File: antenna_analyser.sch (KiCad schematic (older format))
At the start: 25 parts, among them IC1 MCP6002, P1 CONN_01X10, P2 CONN_01X10, P3 CONN_01X04, P4 CONN_01X02

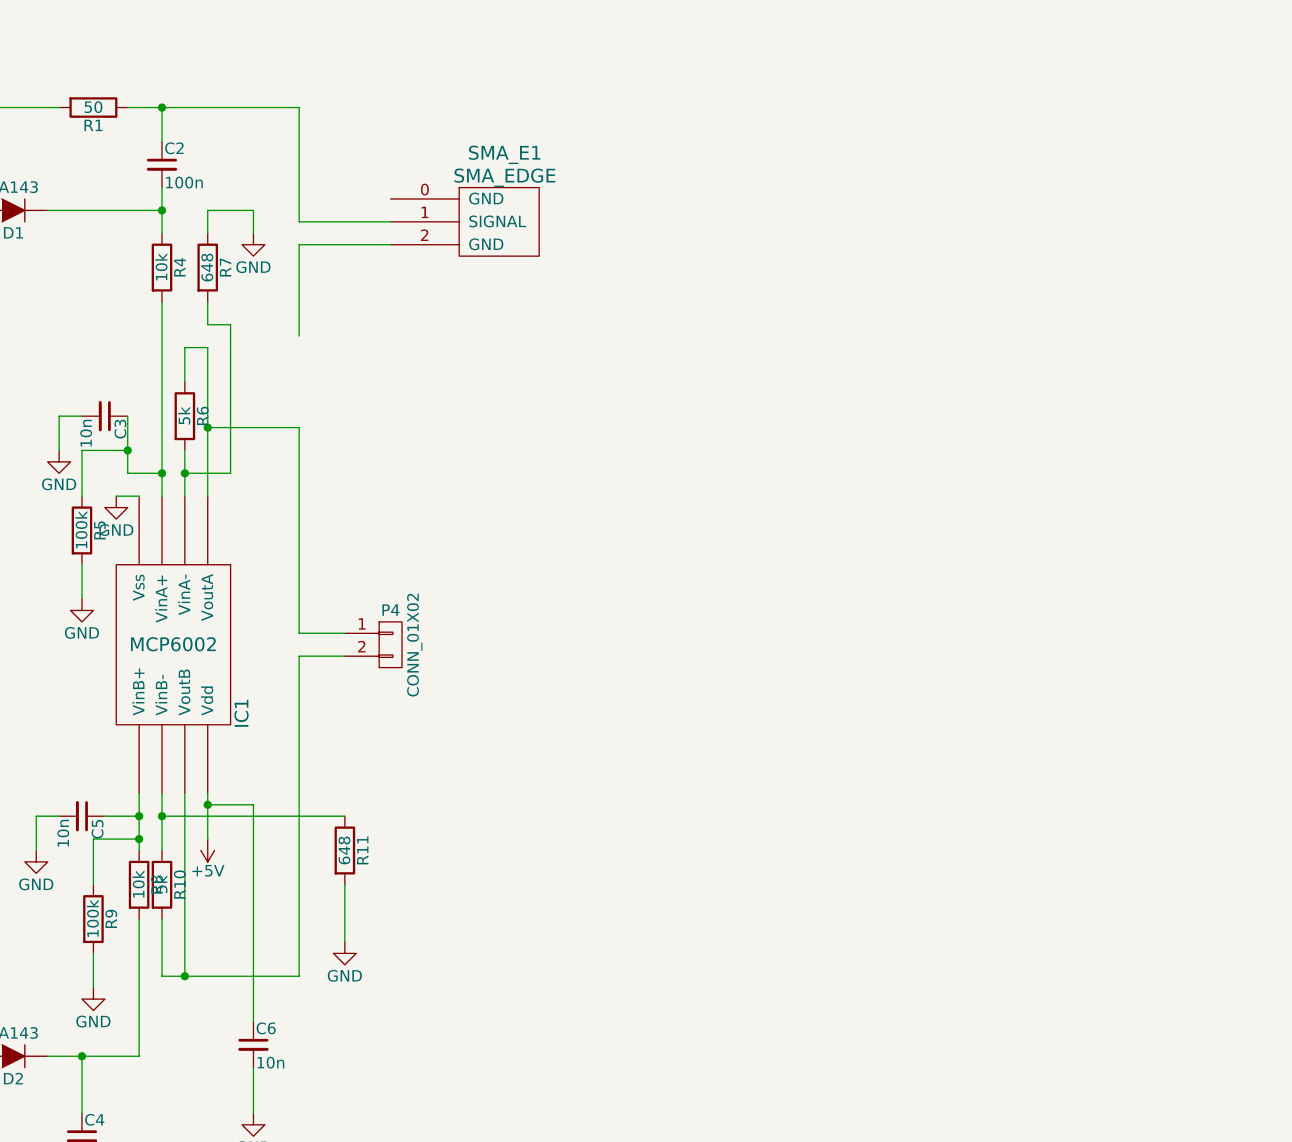
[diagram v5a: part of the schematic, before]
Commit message: Added an Arduino and a voltage regulator to the schematics.
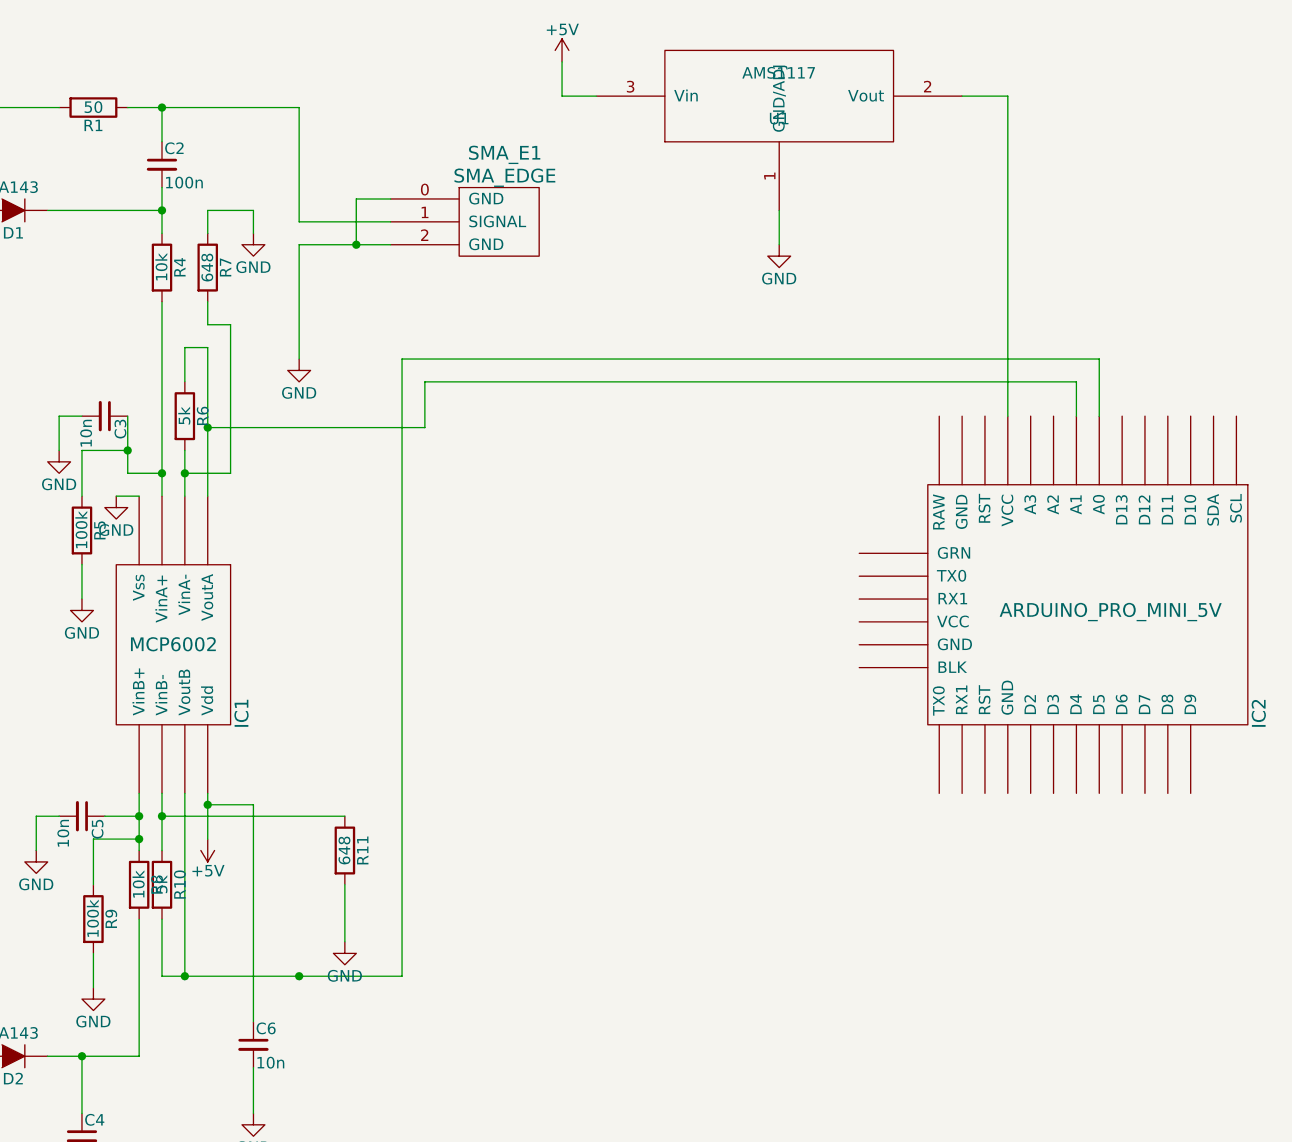
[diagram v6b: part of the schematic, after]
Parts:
- removed P4: CONN_01X02, Pin_Headers:Pin_Header_Straight_1x02, symbol CONN_01X02
- added IC2: ARDUINO_PRO_MINI_5V, arduino pro mini:ARDUINO_PRO_MINI, symbol ARDUINO_PRO_MINI_5V
- added U1: AMS1117, SOT223:SOT223, symbol AMS1117
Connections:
- net +5V: now also U1.3 (Vin)
- net GND: now also SMA_E1.0 (GND), SMA_E1.2 (GND), U1.1 (GND/ADJ)
- net at IC1.~ (Vss), R6.1: now also IC2.~ (VCC)
- net at IC1.~ (Vss), R10.2: now also IC2.~ (VCC)
- new net: IC2.~ (VCC), U1.2 (Vout)
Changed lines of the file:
@@
 LIBS:misc
 LIBS:sma_edge
+LIBS:AMS1117
 LIBS:antenna_analyser-cache
 EELAYER 25 0
@@
 	5250 4950 5250 5200
 Wire Wire Line
-	5250 5200 5850 5200
+	5250 5200 6300 5200
 Wire Wire Line
 	5350 5200 5350 4400
@@
 	5450 4400 5450 4600
 Wire Wire Line
-	5850 2000 5850 2400
+	5850 2000 5850 2500
 Wire Wire Line
 	5250 2250 5250 3100
@@
 	4900 2900 5100 2900
 Connection ~ 5100 2900
-Wire Wire Line
-	5850 3700 5850 2800
-Wire Wire Line
-	5850 2800 5450 2800
 Connection ~ 5450 2800
-Wire Wire Line
-	5850 5200 5850 3800
 Connection ~ 5350 5200
 Wire Wire Line
@@
 Text Notes 2350 4750 0    60   ~ 0
 RESET\nDATA\nCLK\nUPDATE
-$Comp
-L CONN_01X02 P4
-U 1 1 55720A97
-P 6250 3750
-F 0 "P4" H 6250 3900 50  0000 C CNN
-F 1 "CONN_01X02" V 6350 3750 50  0000 C CNN
-F 2 "Pin_Headers:Pin_Header_Straight_1x02" H 6250 3750 60  0001 C CNN
-F 3 "" H 6250 3750 60  0000 C CNN
-	1    6250 3750
-	1    0    0    -1
-$EndComp
-Wire Wire Line
-	5850 3700 6050 3700
-Wire Wire Line
-	5850 3800 6050 3800
 Wire Wire Line
 	5850 1900 6250 1900
@@
 	1    0    0    -1
 $EndComp
+$Comp
+L ARDUINO_PRO_MINI_5V IC2
+U 1 1 558DD335
+P 9250 3600
+F 0 "IC2" H 9700 4400 60  0000 C CNN
+F 1 "ARDUINO_PRO_MINI_5V" V 9250 3750 60  0000 C CNN
+F 2 "arduino pro mini:ARDUINO_PRO_MINI" H 9250 3600 60  0001 C CNN
+F 3 "" H 9250 3600 60  0000 C CNN
+	1    9250 3600
+	0    1    1    0
+$EndComp
+Wire Wire Line
+	9350 2750 9350 2500
+Wire Wire Line
+	9350 2500 6300 2500
+Wire Wire Line
+	6300 2500 6300 5200
+Connection ~ 5850 5200
+Wire Wire Line
+	5450 2800 6400 2800
+Wire Wire Line
+	6400 2800 6400 2600
+Wire Wire Line
+	6400 2600 9250 2600
+Wire Wire Line
+	9250 2600 9250 2750
+$Comp
+L AMS1117 U1
+U 1 1 558DD50C
+P 7950 1350
+F 0 "U1" H 7950 1250 50  0000 C CNN
+F 1 "AMS1117" H 7950 1450 50  0000 C CNN
+F 2 "SOT223:SOT223" H 7950 1350 60  0001 C CNN
+F 3 "" H 7950 1350 60  0000 C CNN
+	1    7950 1350
+	1    0    0    -1
+$EndComp
+$Comp
+L GND #PWR015
+U 1 1 558DD57F
+P 7950 2000
+F 0 "#PWR015" H 7950 1750 50  0001 C CNN
+F 1 "GND" H 7950 1850 50  0000 C CNN
+F 2 "" H 7950 2000 60  0000 C CNN
+F 3 "" H 7950 2000 60  0000 C CNN
+	1    7950 2000
+	1    0    0    -1
+$EndComp
+Wire Wire Line
+	8950 2750 8950 1350
+Wire Wire Line
+	8950 1350 8750 1350
+Wire Wire Line
+	7950 1850 7950 2000
+$Comp
+L +5V #PWR016
+U 1 1 558DD6BD
+P 7000 1200
+F 0 "#PWR016" H 7000 1050 50  0001 C CNN
+F 1 "+5V" H 7000 1340 50  0000 C CNN
+F 2 "" H 7000 1200 60  0000 C CNN
+F 3 "" H 7000 1200 60  0000 C CNN
+	1    7000 1200
+	1    0    0    -1
+$EndComp
+Wire Wire Line
+	7150 1350 7000 1350
+Wire Wire Line
+	7000 1350 7000 1200
+$Comp
+L GND #PWR017
+U 1 1 558DDC04
+P 5850 2500
+F 0 "#PWR017" H 5850 2250 50  0001 C CNN
+F 1 "GND" H 5850 2350 50  0000 C CNN
+F 2 "" H 5850 2500 60  0000 C CNN
+F 3 "" H 5850 2500 60  0000 C CNN
+	1    5850 2500
+	1    0    0    -1
+$EndComp
+Wire Wire Line
+	6250 1800 6100 1800
+Wire Wire Line
+	6100 1800 6100 2000
+Connection ~ 6100 2000
 $EndSCHEMATC

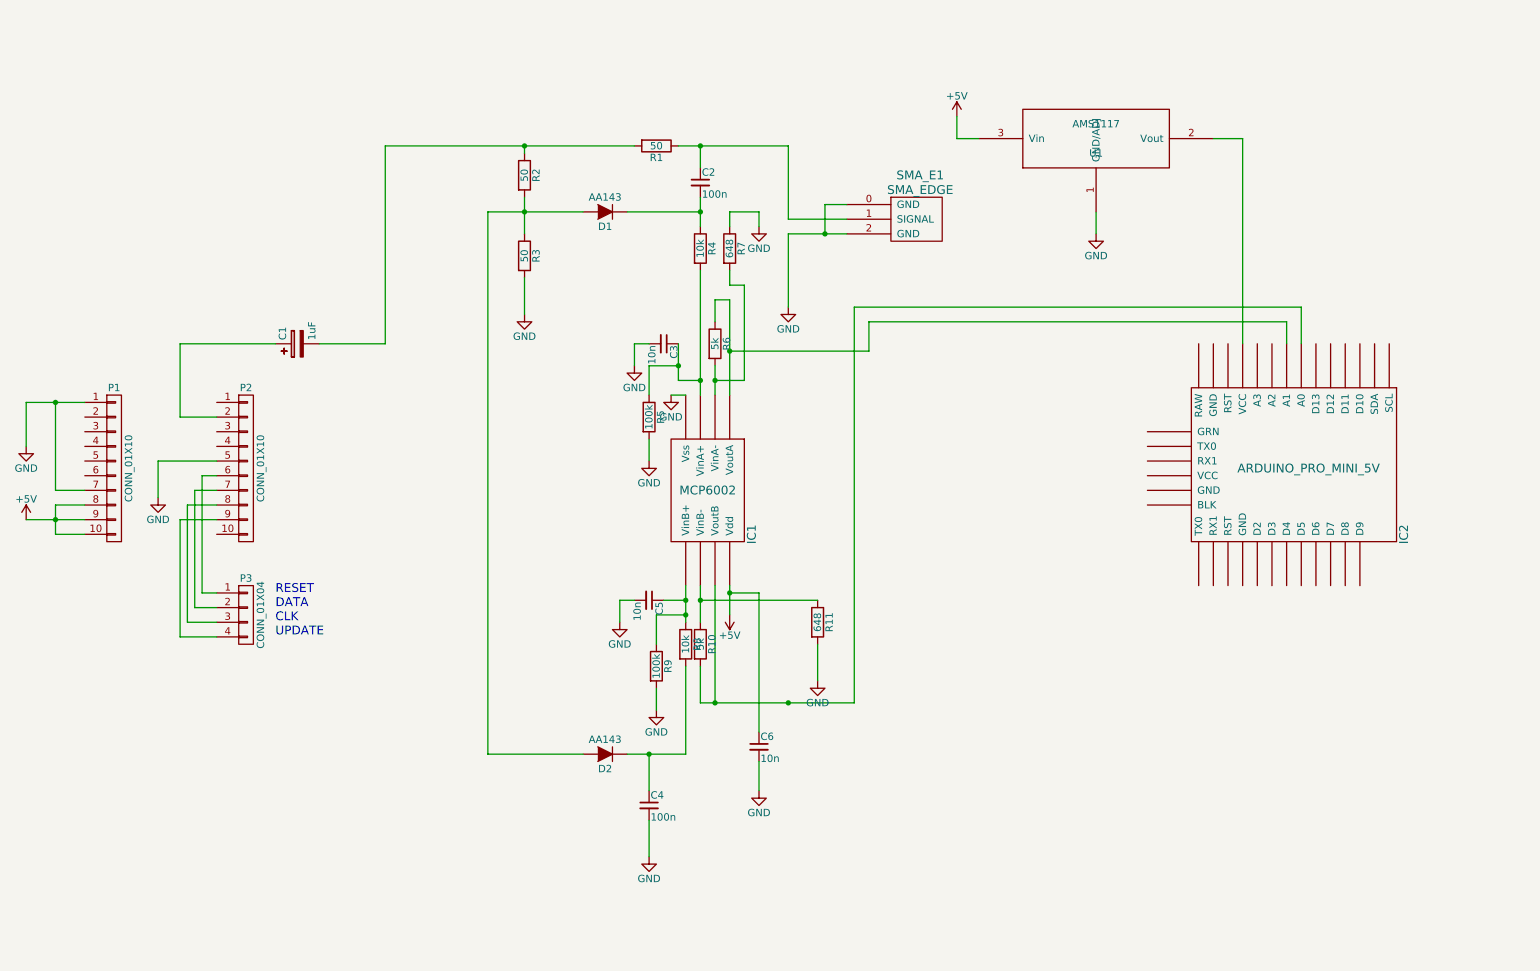
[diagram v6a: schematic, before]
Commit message: Updates to the schematic.
Replaced 50ohm and 5kohm resistors with their equivalent parallel circuits.
Added an AD9850 module to the schematic for easier reference.
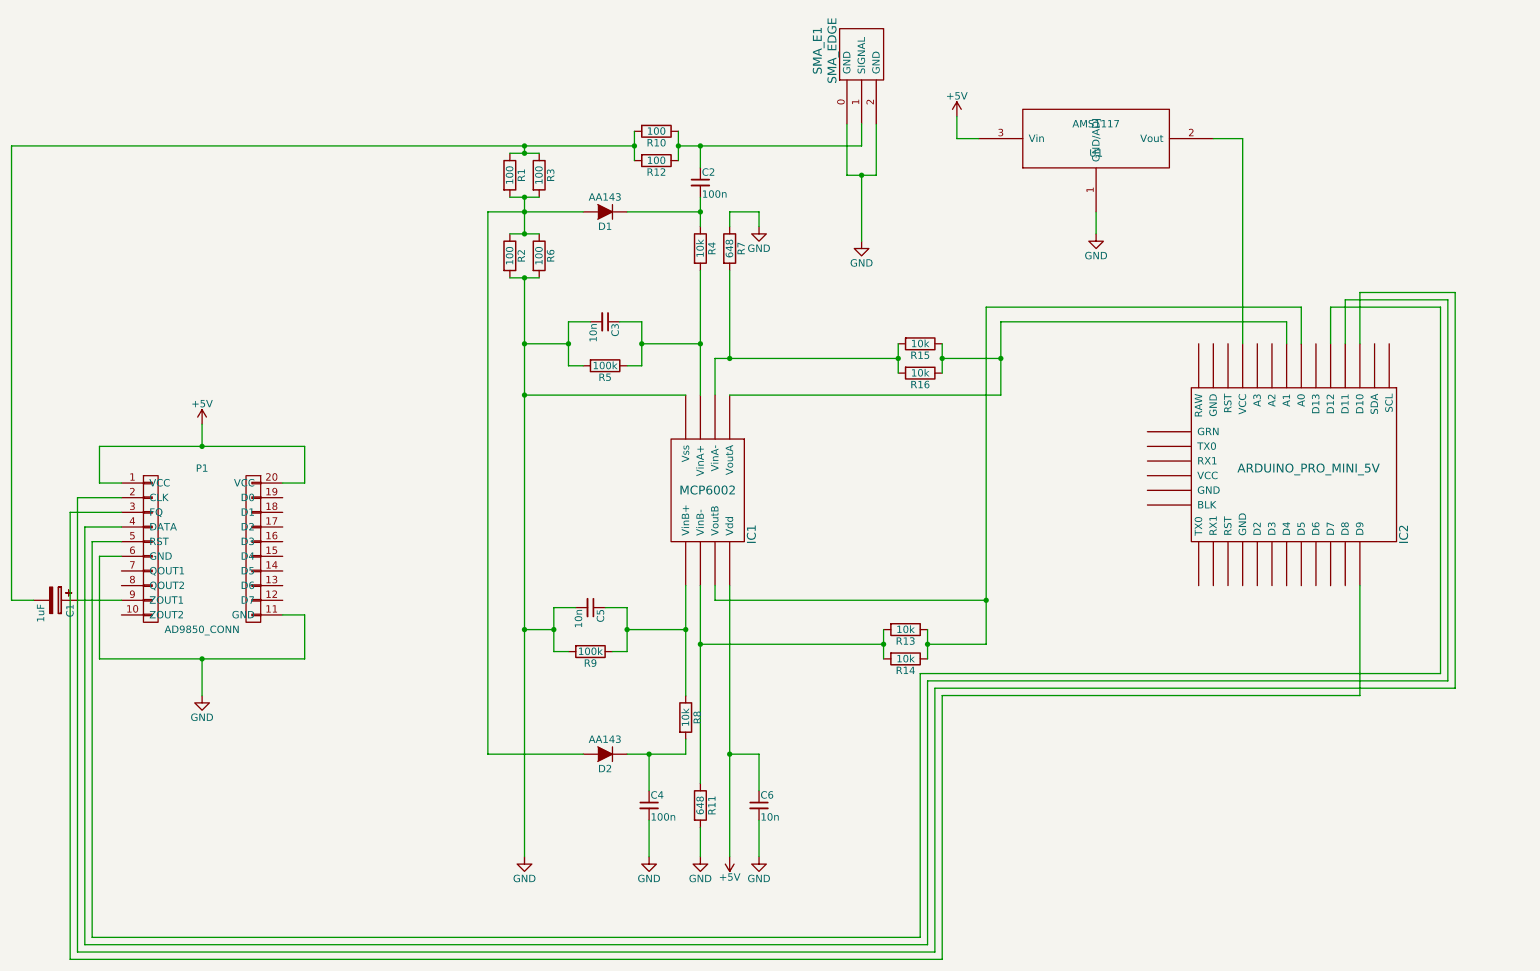
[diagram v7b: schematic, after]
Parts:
- removed P1, P2: CONN_01X10, Pin_Headers:Pin_Header_Straight_1x10, symbol CONN_01X10
- removed P3: CONN_01X04, Pin_Headers:Pin_Header_Straight_1x04, symbol CONN_01X04
- added P1: AD9850_CONN, Pin_Headers:Pin_Header_Straight_1x10, symbol AD9850_CONN
- added R12: 100, Resistors_ThroughHole:Resistor_Horizontal_RM10mm, symbol R
- added R13, R14, R15, R16: 10k, Resistors_ThroughHole:Resistor_Horizontal_RM10mm, symbol R
- R1, R2, R3: value 50 -> 100
- R10, R6: value 5k -> 100
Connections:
- net +5V: now also P1.1 (VCC), P1.20 (VCC)
- net GND: now also R2.2, R6.2, P1.11 (GND), P1.6 (GND); no longer R3.2
- net at D1.2 (A), D2.2 (A): now also R1.2, R2.1, R3.2, R6.1; no longer R2.2, R3.1
- net at C2.1, SMA_E1.1 (SIGNAL): now also R10.1, R12.1; no longer R1.1
- net at C1.1: now also P1.9 (ZOUT1)
- net at IC2.~ (VCC): now also P1.5 (RST)
- new net: C1.2, R1.1, R10.2, R12.2, R3.1
- new net: IC1.~ (Vss), R15.2, R16.2, R7.2
- new net: IC1.~ (Vss), R11.1, R13.2, R14.2
- new net: IC1.~ (Vss), IC2.~ (VCC), R13.1, R14.1
- new net: IC1.~ (Vss), IC2.~ (VCC), R15.1, R16.1
- new net: IC2.~ (VCC), P1.2 (CLK)
- new net: IC2.~ (VCC), P1.3 (FQ)
- new net: IC2.~ (VCC), P1.4 (DATA)
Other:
- note removed: "RESET\nDATA\nCLK\nUPDATE"
- moved on the sheet: C1, C3, C6, R11, R5, R8, SMA_E1
